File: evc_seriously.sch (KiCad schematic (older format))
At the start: 23 parts

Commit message: Add more library parts, add parts to schematic
- Added a new project-level library to contain new parts:
  - MIC2981 source driver
  - LM9022 filament driver
  - TCA9517 I2C bus repeater
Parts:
- added U?: LM9022, symbol evc_seriously:LM9022
- added U?: TCA9517, symbol evc_seriously:TCA9517
- added U?: MIC2981, symbol evc_seriously:MIC2981
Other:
- note removed: "some random LT boost part"
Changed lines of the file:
@@
 U 1 1 5F7AE5D9
 P 4500 3250
-F 0 "U?" H 4450 2161 50  0000 C CNN
-F 1 "STM32F303K8Tx" H 4450 2070 50  0000 C CNN
+F 0 "U?" H 4050 4100 50  0000 C CNN
+F 1 "STM32F303K8Tx" H 4000 2300 50  0000 C CNN
 F 2 "Package_QFP:LQFP-32_7x7mm_P0.8mm" H 4000 2350 50  0001 R CNN
 F 3 "http://www.st.com/st-web-ui/static/active/en/resource/technical/document/datasheet/DM00092070.pdf" H 4500 3250 50  0001 C CNN
@@
 	1    0    0    -1
 $EndComp
-Text Notes 7800 4850 0    50   ~ 0
+Text Notes 2750 7250 0    50   ~ 0
 TCA9517 I2C bus repeater
 Text Notes 7850 4950 0    50   ~ 0
 MPS3510A monolithic buck regulator
-Text Notes 7950 5050 0    50   ~ 0
+Text Notes 4550 6800 0    50   ~ 0
 MIC2981 8-channel high voltage source driver
-Text Notes 8050 5150 0    50   ~ 0
-some random LT boost part
 $Comp
 L Switch:SW_Push SW?
@@
 	1    0    0    -1
 $EndComp
-Text Notes 8200 5250 0    50   ~ 0
+Text Notes 2700 5950 0    50   ~ 0
 LM4781/LM9022 filament driver
 $Comp
 L Connector:USB_B_Mini J?
 U 1 1 5F7B8668
-P 4500 5400
-F 0 "J?" H 4557 5867 50  0000 C CNN
-F 1 "USB_B_Mini" H 4557 5776 50  0000 C CNN
-F 2 "" H 4650 5350 50  0001 C CNN
-F 3 "~" H 4650 5350 50  0001 C CNN
-	1    4500 5400
+P 9550 1950
+F 0 "J?" H 9607 2417 50  0000 C CNN
+F 1 "USB_B_Mini" H 9607 2326 50  0000 C CNN
+F 2 "" H 9700 1900 50  0001 C CNN
+F 3 "~" H 9700 1900 50  0001 C CNN
+	1    9550 1950
 	1    0    0    -1
 $EndComp
@@
 L Jumper:SolderJumper_2_Bridged JP?
 U 1 1 5F80C17D
-P 7050 1100
-F 0 "JP?" H 7050 1305 50  0000 C CNN
-F 1 "SolderJumper_2_Bridged" H 7050 1214 50  0000 C CNN
-F 2 "" H 7050 1100 50  0001 C CNN
-F 3 "~" H 7050 1100 50  0001 C CNN
-	1    7050 1100
+P 2950 4750
+F 0 "JP?" H 2950 4955 50  0000 C CNN
+F 1 "SolderJumper_2_Bridged" H 2950 4864 50  0000 C CNN
+F 2 "" H 2950 4750 50  0001 C CNN
+F 3 "~" H 2950 4750 50  0001 C CNN
+	1    2950 4750
 	1    0    0    -1
 $EndComp
@@
 L Jumper:SolderJumper_2_Bridged JP?
 U 1 1 5F80C42A
-P 7050 1250
-F 0 "JP?" H 7050 1455 50  0000 C CNN
-F 1 "SolderJumper_2_Bridged" H 7050 1364 50  0000 C CNN
-F 2 "" H 7050 1250 50  0001 C CNN
-F 3 "~" H 7050 1250 50  0001 C CNN
-	1    7050 1250
-	1    0    0    -1
-$EndComp
+P 2950 4900
+F 0 "JP?" H 2950 5105 50  0000 C CNN
+F 1 "SolderJumper_2_Bridged" H 2950 5014 50  0000 C CNN
+F 2 "" H 2950 4900 50  0001 C CNN
+F 3 "~" H 2950 4900 50  0001 C CNN
+	1    2950 4900
+	1    0    0    -1
+$EndComp
+$Comp
+L evc_seriously:LM9022 U?
+U 1 1 5F7BF1AB
+P 3250 5450
+F 0 "U?" H 2900 5800 50  0000 C CNN
+F 1 "LM9022" H 3000 5100 50  0000 C CNN
+F 2 "" H 3250 5450 50  0001 C CNN
+F 3 "" H 3250 5450 50  0001 C CNN
+	1    3250 5450
+	1    0    0    -1
+$EndComp
+$Comp
+L evc_seriously:TCA9517 U?
+U 1 1 5F7CAC11
+P 3250 6700
+F 0 "U?" H 2900 7050 50  0000 C CNN
+F 1 "TCA9517" H 3000 6350 50  0000 C CNN
+F 2 "" H 3250 6700 50  0001 C CNN
+F 3 "" H 3250 6700 50  0001 C CNN
+	1    3250 6700
+	1    0    0    -1
+$EndComp
+$Comp
+L evc_seriously:MIC2981 U?
+U 1 1 5F8198FC
+P 5300 6000
+F 0 "U?" H 4900 6550 50  0000 C CNN
+F 1 "MIC2981" H 5000 5450 50  0000 C CNN
+F 2 "" H 5300 6000 50  0001 C CNN
+F 3 "" H 5300 6000 50  0001 C CNN
+	1    5300 6000
+	1    0    0    -1
+$EndComp

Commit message: Majority of schematic capture complete
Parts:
- removed J?: USB_B_Mini, symbol Connector:USB_B_Mini
- removed JP? (x2): SolderJumper_2_Bridged, symbol Jumper:SolderJumper_2_Bridged
- removed R? (x3): R, symbol Device:R
- added C?: 1uF, symbol Device:C
- added C? (x2): 22pF, symbol Device:C_Small
- added JP? (x2): SolderJumper_2_Open, symbol Jumper:SolderJumper_2_Open
- added R? (x3): 10k, symbol Device:R
- added R? (x2): 22, symbol Device:R
- added R? (x2): 75k, symbol Device:R
- added R?: 24k, symbol Device:R
- added R?: 14.3k, symbol Device:R
- added R?: 1M, symbol Device:R
- added U? (x2): MPM3510A, symbol evc_seriously:MPM3510A
- J?: value Conn_02x05_Counter_Clockwise -> J_OUT
- J?: value Conn_02x05_Counter_Clockwise -> J_IN
- R? (x2): value R -> 10k
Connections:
- net labels added: 3V3_B, 5V_EN, FIL_PWM, GRID, I2C_EN, NRST, SCL_A, SCL_B, SDA_A, SDA_B, SEG_A, SEG_B, SEG_C, SEG_D, SEG_E, SEG_F, SEG_G, SWDCLK, SWDIO, SWO, VFIL+, VFIL-
- wire segments 0 -> 164
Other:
- note added: "SDx_A: I2C from previous board in chain\nSDx_B: I2C to next board in chain\n3V3_B: +3.3V rail from next board in chain"
- moved on the sheet: D?, J?, R?, SW?, TP?, U?

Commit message: Finish schematic capture
- Can I interest you in some capacitors?
- Perhaps some pullup/pulldowns?
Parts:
- added C? (x2): 4.7uF, symbol Device:C
- added C? (x2): 22uF, symbol Device:C
- added C? (x6): 0.1uF, symbol Device:C
- added R? (x6): 10k, symbol Device:R
- added R?: 22, symbol Device:R
- R? (x2): value R -> 660
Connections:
- net +24V: now also TP?.1, C?.2, C?.2, C?.2
- net +3V3: now also J?.6 (Pin_6), R?.2, TP?.1, C?.2, C?.2, C?.2, C?.2, R?.1, R?.1, R?.1; no longer J?.8 (Pin_8)
- net +5V: now also TP?.1, C?.2, C?.2
- net 5V_EN: now also U?.27 (PB4), R?.1; no longer U?.2 (PF0)
- net GND: now also D?.1 (K), D?.1 (K), SW?.2, TP?.1, C?.1, C?.1, C?.1, C?.1, C?.1, C?.1, C?.1, C?.1, C?.1, C?.1, R?.1, R?.2, R?.2
- net I2C_EN: now also U?.28 (PB5), R?.1; no longer U?.3 (PF1)
- net SCL_A: now also J?.7 (Pin_7), R?.2; no longer J?.6 (Pin_6)
- net SCL_B: now also J?.7 (Pin_7); no longer J?.6 (Pin_6)
- net SDA_A: now also J?.8 (Pin_8), R?.2; no longer J?.7 (Pin_7)
- net SDA_B: now also J?.8 (Pin_8); no longer J?.7 (Pin_7)
- net SWO: now also U?.26 (PB3)
- net USR_SW: now reaches U?.20 (PA10)
- net USR_SW: now also SW?.1, R?.2
- net USR_LED: now reaches U?.21 (PA11)
- net USR_LED: now also R?.2
- net at D?.2 (A): now also R?.1 (x2)
- net +3V3_B: now reaches TP?.1
- net +3V3_B: now also J?.6 (Pin_6), U?.8 (VCCB), C?.2, R?.2, R?.2
- removed net 3V3_B: J?.8 (Pin_8), U?.8 (VCCB)
- new net: R?.1, U?.3 (PF1)
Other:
- note removed: "* using +24V adapter so we can eliminate the +12V rail and boost converter"
- moved on the sheet: D?, R?, SW?, TP?

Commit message: Minor changes to please ERC
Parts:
- gave numbers to parts that had none: 54
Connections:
- no-connect marks 0 -> 14
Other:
- moved on the sheet: C1, C10, C11, C2, C3, C4, C5, C6, C7, C9, TP1, TP2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

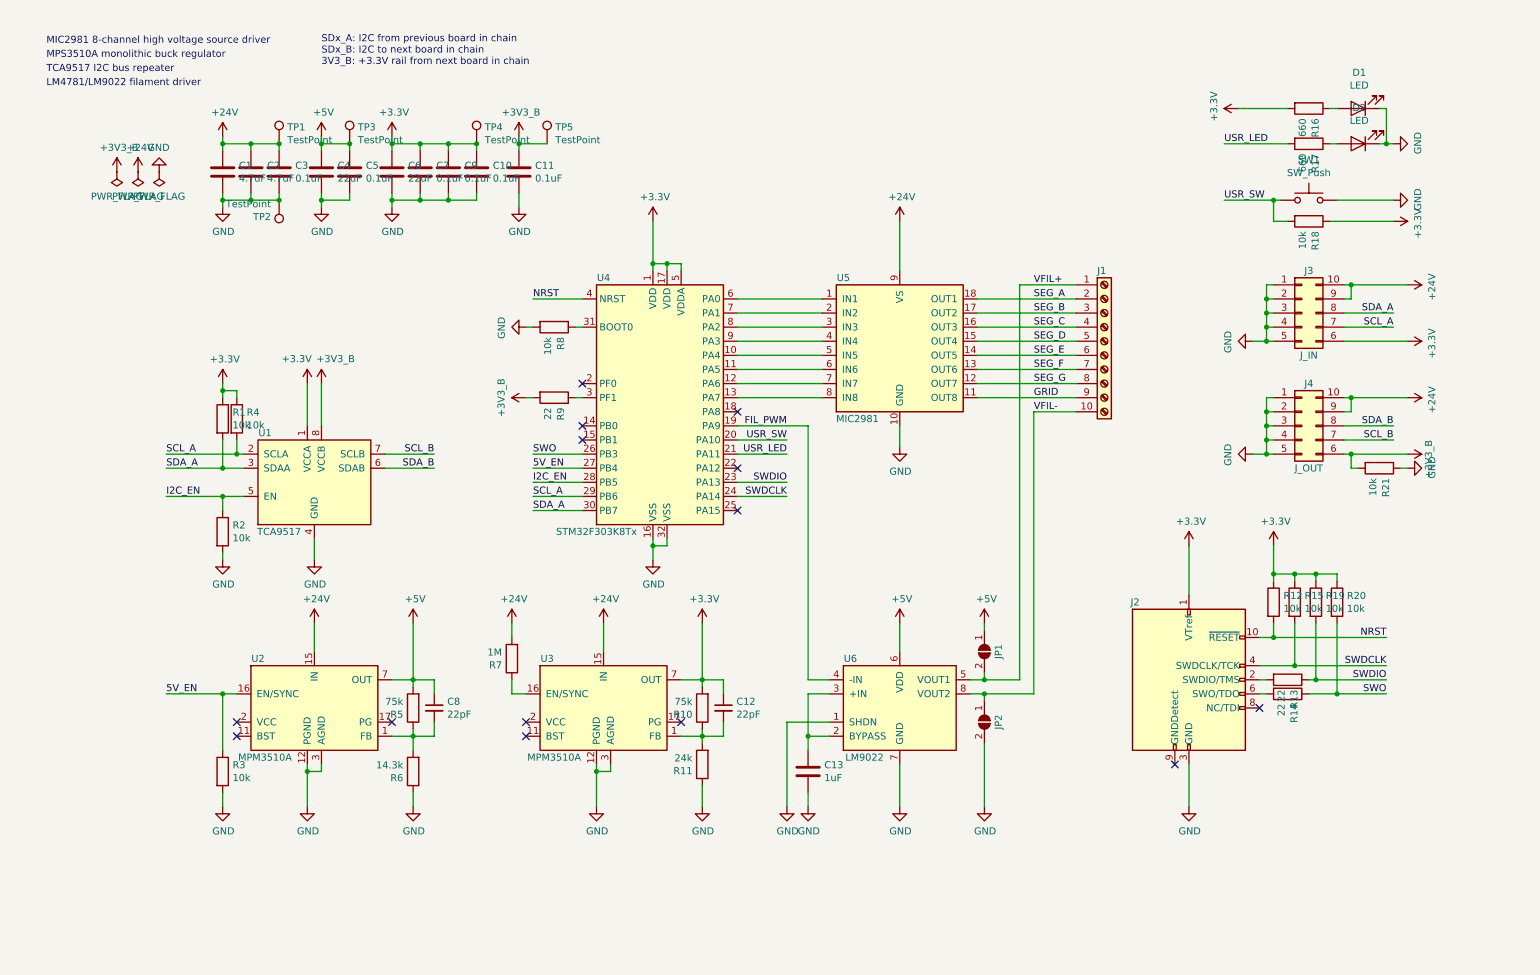
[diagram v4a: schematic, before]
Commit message: Tidy schematic
I'm really just stalling to avoid creating footprints
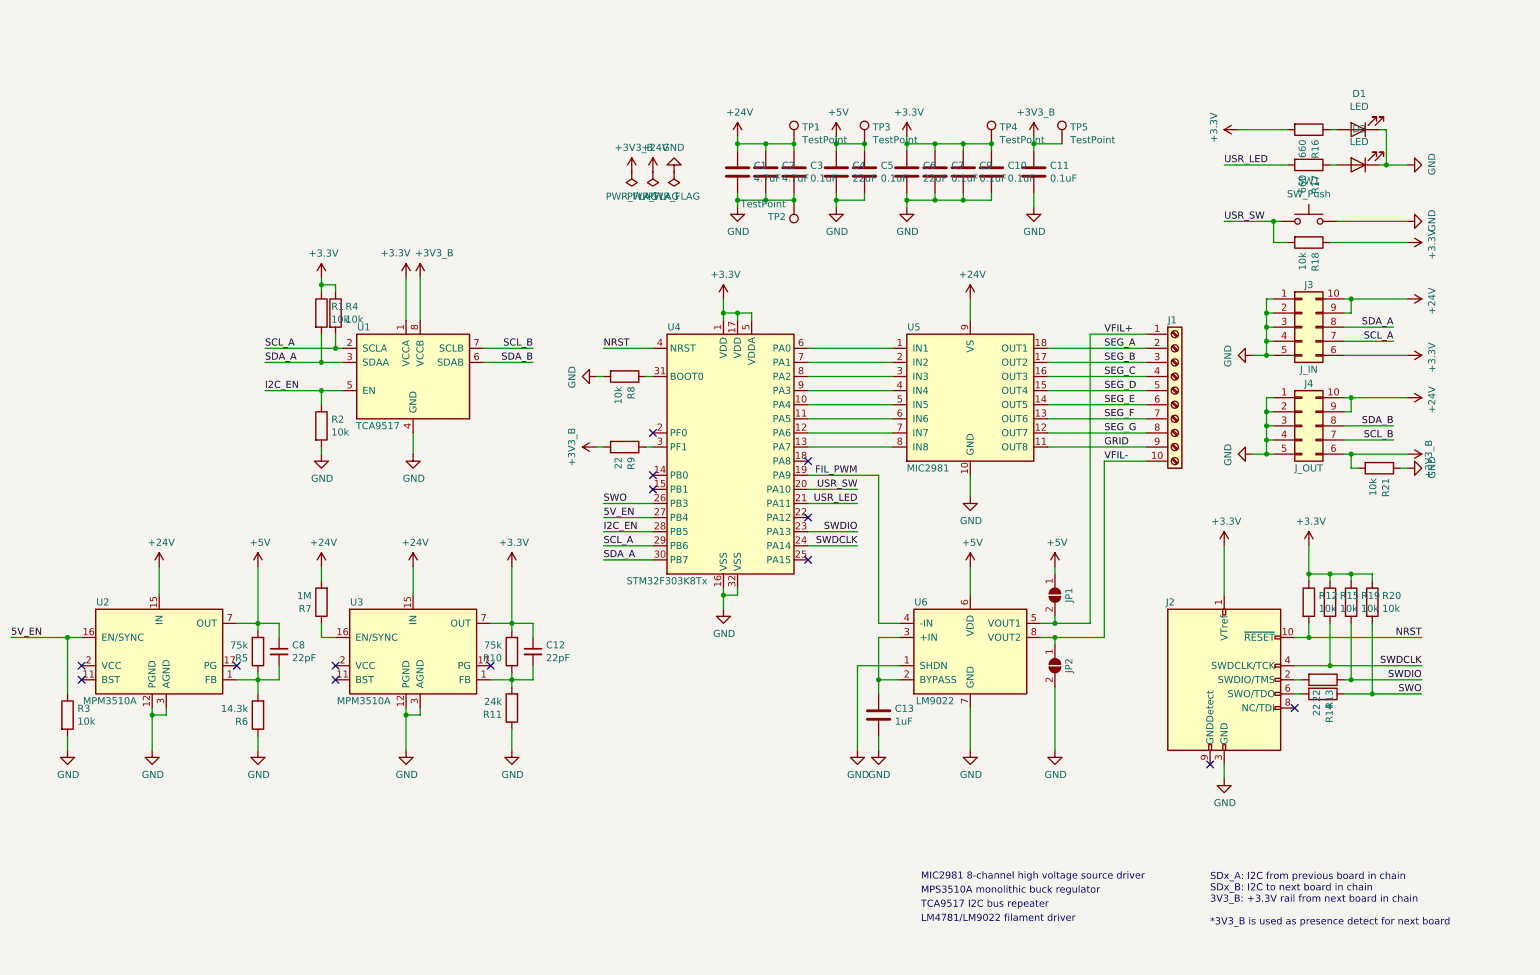
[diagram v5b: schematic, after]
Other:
- note added: "SDx_A: I2C from previous board in chain\nSDx_B: I2C to next board in chain\n3V3_B: +3.3V rail from next board in chain\n\n*3V3_B is used as presence detect for next board"
- note removed: "SDx_A: I2C from previous board in chain\nSDx_B: I2C to next board in chain\n3V3_B: +3.3V rail from next board in chain"
- moved on the sheet: C1, C10, C11, C12, C13, C2, C3, C4, C5, C6, C7, C8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

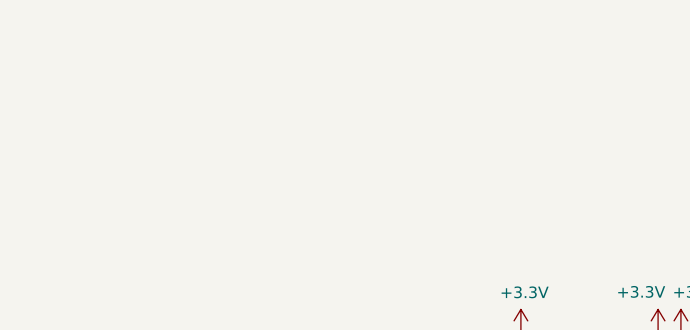
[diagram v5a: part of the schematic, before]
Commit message: Add final footprints, begin routing board
Assign footprints to components, tune up some footprints/symbols
Add missing footprint for MPM3510A
Start placing components and routing board
HOLY CATS that buck regulator part was a pain to create a footprint for!
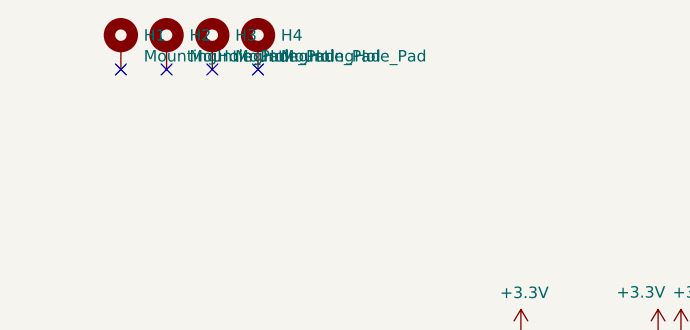
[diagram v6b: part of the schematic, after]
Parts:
- added H1, H2, H3, H4: MountingHole_Pad, MountingHole:MountingHole_3.2mm_M3_Pad, symbol Mechanical:MountingHole_Pad
- C1, C2, C4, C6: footprint (none) -> Capacitor_SMD:CP_Elec_5x5.8
- C10, C11, C12, C13, C3, C5, C7, C8, C9: footprint (none) -> Capacitor_SMD:C_0603_1608Metric
- D1, D2: footprint (none) -> LED_SMD:LED_0805_2012Metric
- J1: footprint (none) -> Connector_Phoenix_MSTB:PhoenixContact_MSTBVA_2,5_10-G_1x10_P5.00mm_Vertical
- J2: footprint (none) -> Connector_PinHeader_1.27mm:PinHeader_2x05_P1.27mm_Vertical
- J3, J4: footprint (none) -> Connector_PinHeader_2.54mm:PinHeader_2x05_P2.54mm_Vertical
- JP1, JP2: footprint (none) -> Jumper:SolderJumper-2_P1.3mm_Open_TrianglePad1.0x1.5mm
- R1, R10, R11, R12, R13, R14, R15, R16, R17, R18, R19, R2, R20, R21, R3, R4, R5, R6, R7, R8, R9: footprint (none) -> Resistor_SMD:R_0603_1608Metric
- SW1: footprint (none) -> Button_Switch_SMD:Panasonic_EVQPUK_EVQPUB
- TP1, TP2, TP3, TP4, TP5: footprint (none) -> TestPoint:TestPoint_Pad_D1.0mm
- U1: footprint (none) -> Package_SO:SOIC-8_3.9x4.9mm_P1.27mm
- U2, U3: footprint (none) -> evc_seriously:QFN-19_3x5mm_P0.6mm
- U5: footprint (none) -> Package_SO:SOIC-18W_7.5x11.6mm_P1.27mm
- U6: footprint (none) -> Package_SO:SO-8_3.9x4.9mm_P1.27mm
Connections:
- no-connect marks 14 -> 18

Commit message: More routing of the board
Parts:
- C1, C2: footprint Capacitor_SMD:CP_Elec_5x5.8 -> Capacitor_SMD:C_0805_2012Metric
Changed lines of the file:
@@
 F 0 "C1" H 5635 1604 50  0000 R CNN
 F 1 "4.7uF" H 5635 1695 50  0000 R CNN
-F 2 "Capacitor_SMD:CP_Elec_5x5.8" H 5788 1500 50  0001 C CNN
+F 2 "Capacitor_SMD:C_0805_2012Metric" H 5788 1500 50  0001 C CNN
 F 3 "~" H 5750 1650 50  0001 C CNN
 	1    5750 1650
@@
 F 0 "C2" H 5835 1604 50  0000 R CNN
 F 1 "4.7uF" H 5835 1695 50  0000 R CNN
-F 2 "Capacitor_SMD:CP_Elec_5x5.8" H 5988 1500 50  0001 C CNN
+F 2 "Capacitor_SMD:C_0805_2012Metric" H 5988 1500 50  0001 C CNN
 F 3 "~" H 5950 1650 50  0001 C CNN
 	1    5950 1650
